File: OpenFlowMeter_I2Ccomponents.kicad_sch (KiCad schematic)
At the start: 10 parts, among them U10 BME680, U7 24LC64, U9 TMP100

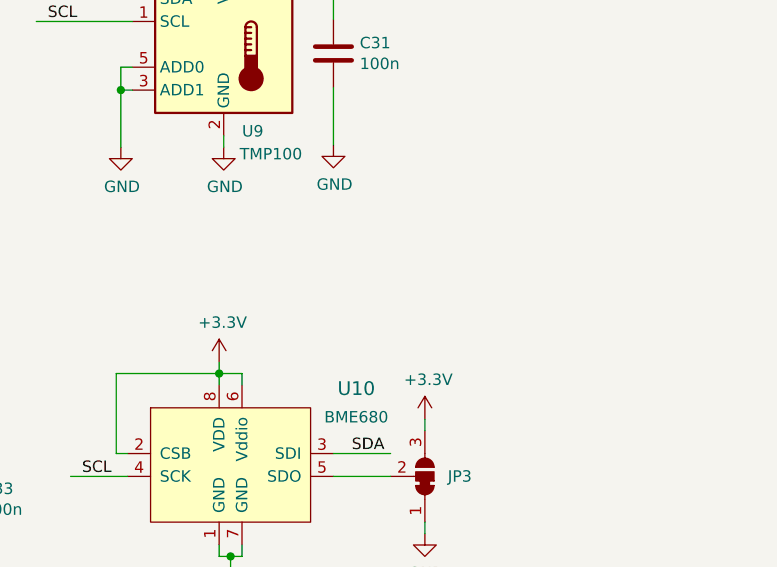
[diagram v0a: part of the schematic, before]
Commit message: added some notes regarding production changes
Some changes, because I did not had the right parts in my hands, some because I wanted to try different ones.
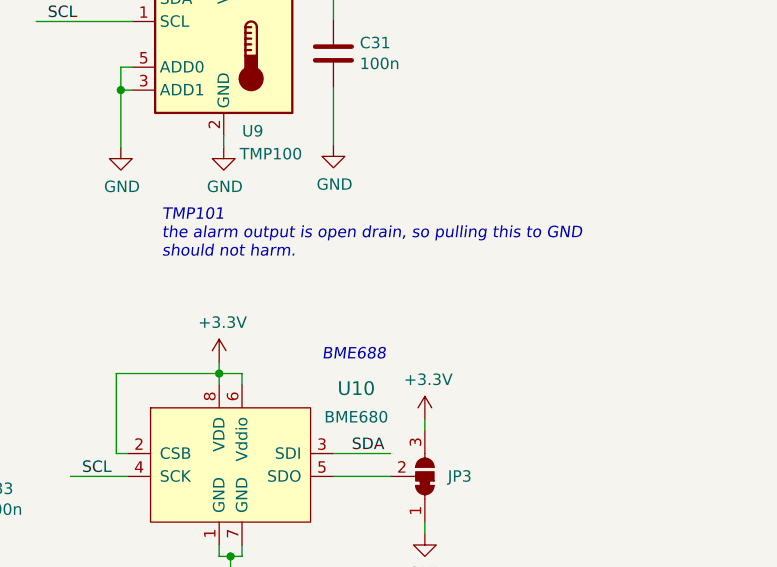
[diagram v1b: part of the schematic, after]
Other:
- note added: "BME688"
- note added: "TMP101 the alarm output is open drain, so pulling this to GND should not harm."
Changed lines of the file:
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@@
     (effects (font (size 1.27 1.27)) (justify left bottom))
+  )
+  (text "BME688" (at 246.38 129.54 0)
+    (effects (font (size 1.27 1.27) italic) (justify left bottom))
+  )
+  (text "TMP101\nthe alarm output is open drain, so pulling this to GND\nshould not harm."
+    (at 228.6 118.11 0)
+    (effects (font (size 1.27 1.27) italic) (justify left bottom))
   )
   (label "SCL" (at 219.71 142.24 0)

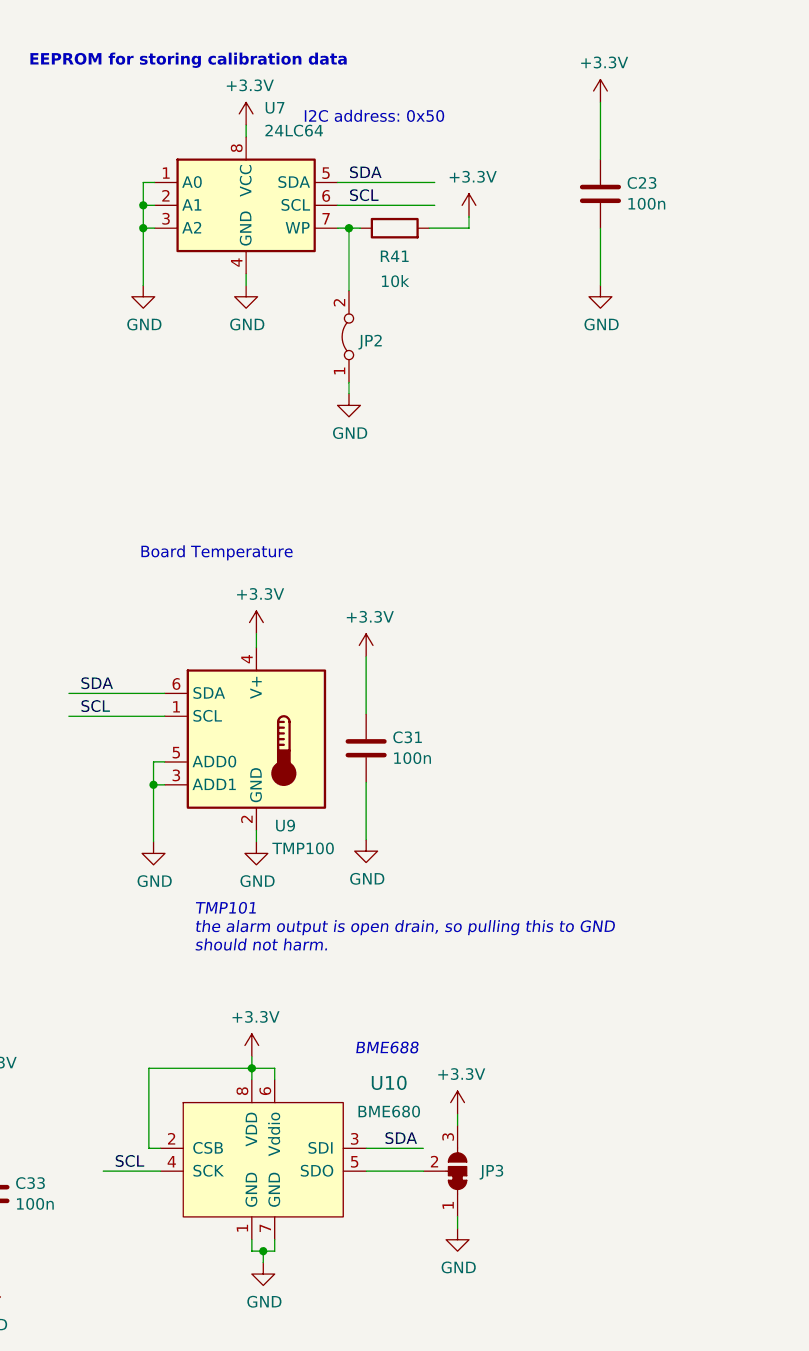
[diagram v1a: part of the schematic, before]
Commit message: converted project into KiCAD 6.99
using 6.99.0-5192-g5e0064c21e release build, just to test the "new features"
adapted page numbering (current source 1 was page 4 and CS 2 page 3)
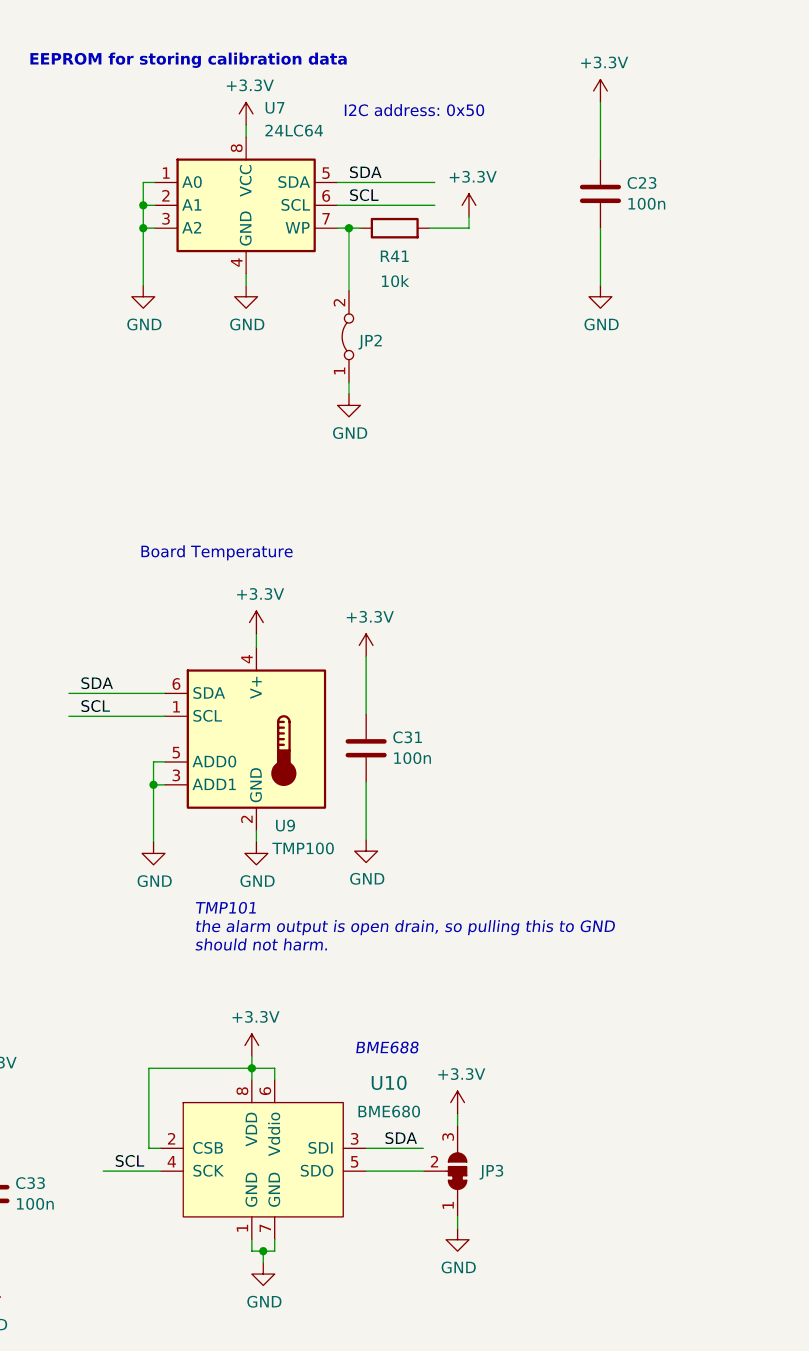
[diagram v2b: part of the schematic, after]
